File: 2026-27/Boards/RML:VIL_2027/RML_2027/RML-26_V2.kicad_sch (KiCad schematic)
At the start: 28 parts, among them J1 043045-0412, Q2 AO3400A, Q3 UJ3N065080K3S, Q4 AO3401A, U1 H11L1, U2 LMC555CMX/NOPB

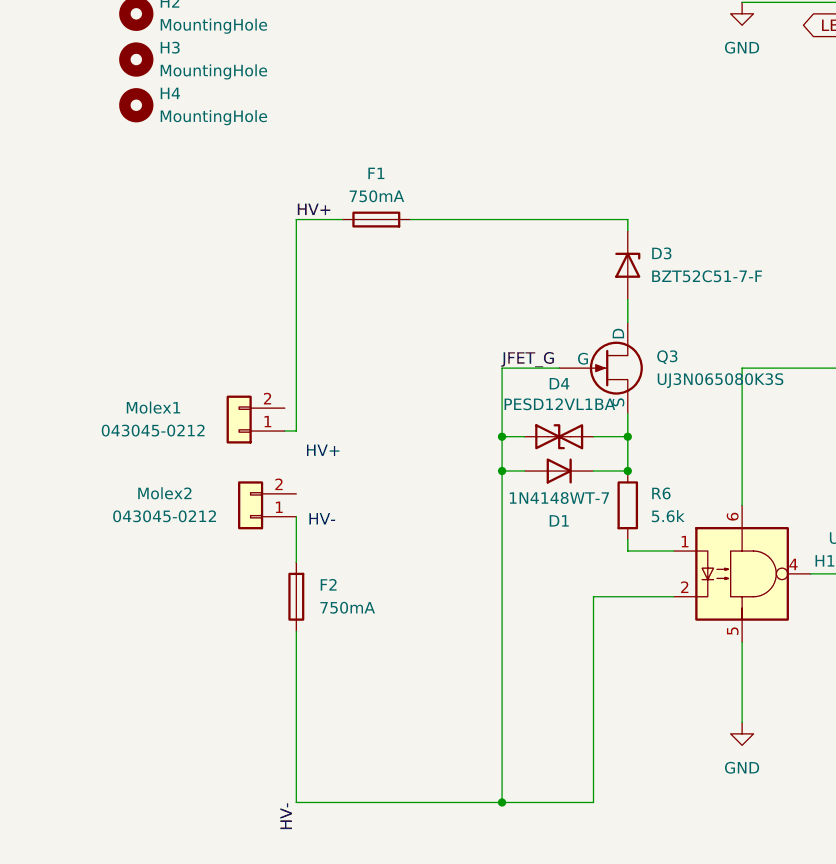
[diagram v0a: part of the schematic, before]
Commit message: Update SDC and CAN schematics and RML 2027 board files
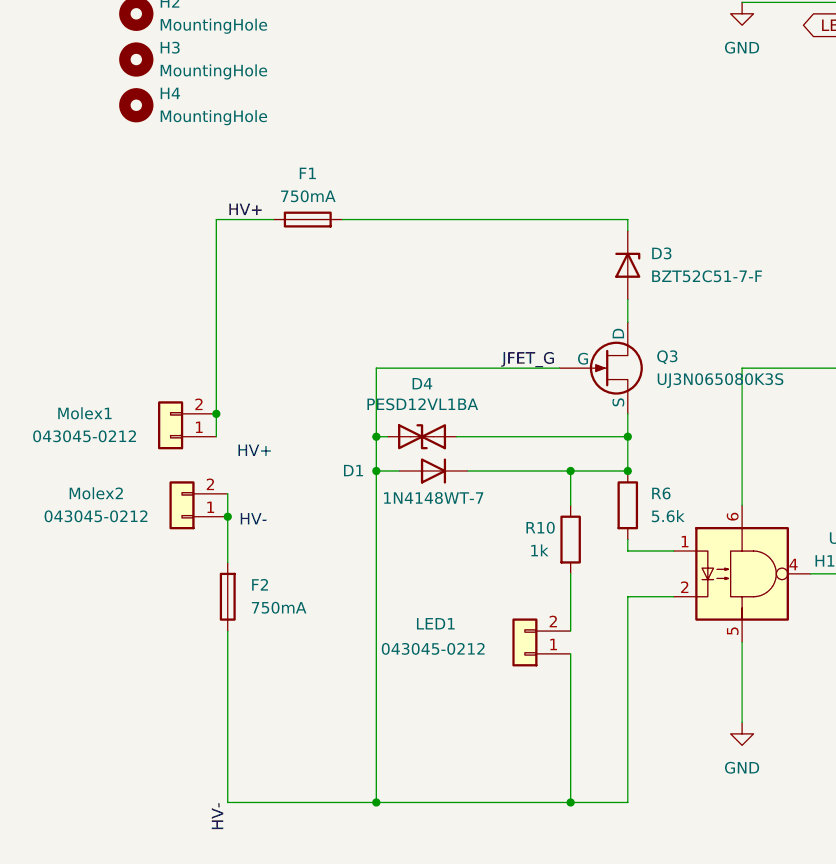
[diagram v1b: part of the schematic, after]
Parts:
- added LED1: 043045-0212, Connector_Molex:Molex_Micro-Fit_3.0_43045-0212_2x01_P3.00mm_Vertical, symbol Connector_Generic:Conn_01x02
- added R10: 1k, Resistor_SMD:R_0805_2012Metric_Pad1.20x1.40mm_HandSolder, symbol Device:R
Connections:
- net HV+: now also Molex1.2 (Pin_2)
- net HV-: now also LED1.1 (Pin_1)
- net at D1.1 (K), D4.1 (A1), Q3.3 (S)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: now also R10.1
- net at F2.2, Molex2.1 (Pin_1): now also Molex2.2 (Pin_2)
- new net: LED1.2 (Pin_2), R10.2
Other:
- moved on the sheet: D1, D4, F1, F2, Molex1, Molex2
